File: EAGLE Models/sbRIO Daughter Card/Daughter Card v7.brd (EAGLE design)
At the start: 120.7 x 102.9 mm, 88 parts, among them IC1 BTS716G, IC2 BTS716G, IC3 BTS716G

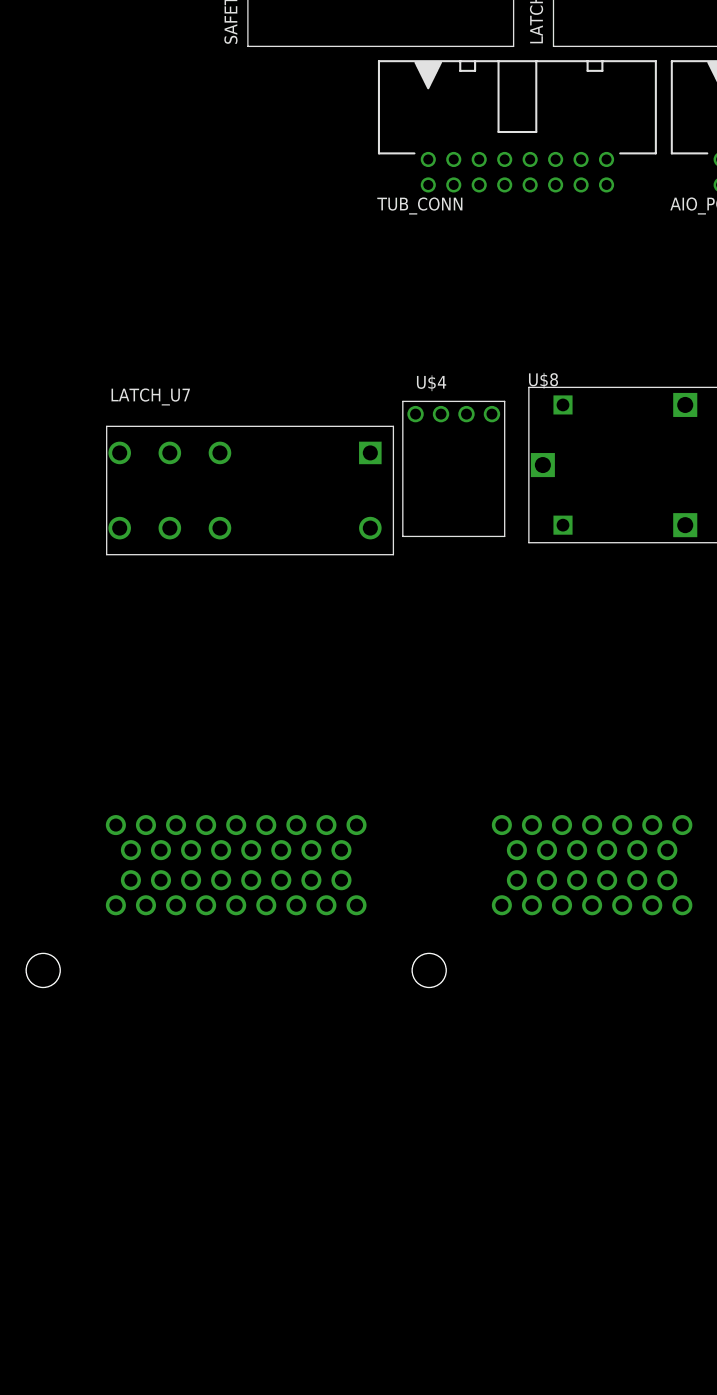
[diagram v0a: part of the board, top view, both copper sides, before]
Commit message: Began Seriously reworking Daughter card and tracing nets to new connectors
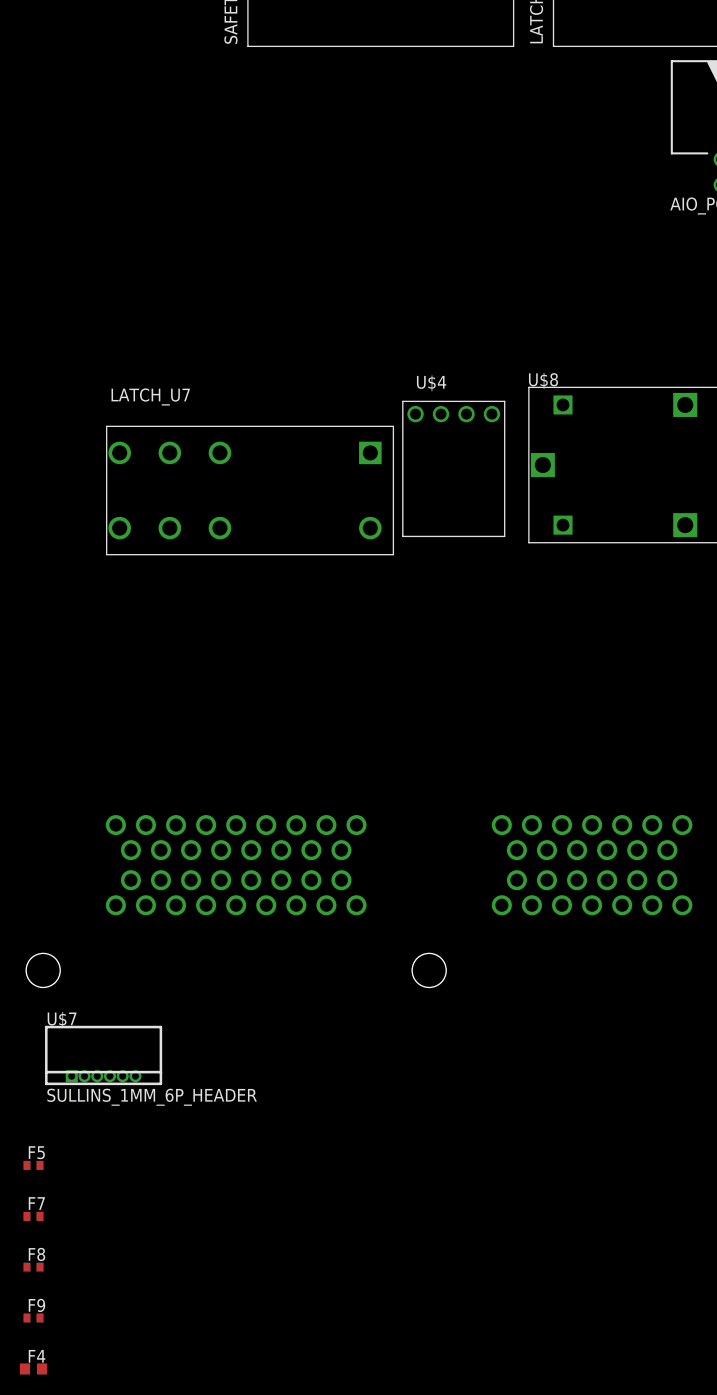
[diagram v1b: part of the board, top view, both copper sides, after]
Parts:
- removed TUB_CONN: 2516-5, con-3m:PAK100/2500-5-16
- added F4: 0.5A PTC, resistor:R0603
- added F5, F7, F8, F9: 10mA PTC, resistor:R0402
- added U$7: SULLINS_1MM_6P_HEADER, formula electric:SULLINS_1MM_HEADER
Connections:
- new net BRAKELIGHT: U$6.A17
- new net COOLANT_PUMP: AIO_PO_CONN.13
- new net FAN_PWM_OUT: AIO_PO_CONN.16
- new net N$11: U$6.A22
- new net N$12: F4.2
- new net N$15: U$6.B3
- new net N$16: U$6.A4
- new net N$17: U$6.A5
- new net N$18: U$6.A6
- new net N$19: U$6.A7
- new net N$21: U$6.A8
- new net N$22: U$6.A9
- new net N$23: U$6.B4
- new net N$24: U$6.B5
- new net N$25: U$6.B6
- new net N$26: U$6.B7
- new net N$28: U$6.A19
- new net N$30: U$6.A20
- new net N$31: U$6.B9
- new net N$32: U$6.B10
- new net N$33: U$6.A23
- new net N$34: U$6.A24
- new net N$35: U$6.A25
- new net N$36: U$6.A26
- new net N$37: U$6.A27
- new net N$38: U$6.A28
- new net N$39: U$6.A29
- new net N$40: U$6.A30
- new net N$42: U$6.A31
- new net N$43: U$6.A32
- new net N$44: U$6.A33
- new net N$45: U$6.A34
- new net N$67: U$6.B11
- new net N$68: U$6.B12
- new net N$69: U$6.B13
- new net N$70: F5.2
- new net N$71: F7.2
- new net N$72: F8.2
- new net N$73: F9.2
- net 5V: now also F4.1
- net 5V_IO_1: no longer TUB_CONN.3
- net ACCUMULATOR_FANS: now also AIO_PO_CONN.15; no longer AIO_PO_CONN.16
- net AI7: now also U$6.A11; no longer TUB_CONN.15
- net AMS_OUT: no longer TUB_CONN.6
- net AO0: now also F5.1
- net AO1: now also F7.1
- net AO2: now also F8.1
- net AO3: now also F9.1
- net BRAKE_PRESS_IN_1: now also U$6.A15; no longer TUB_CONN.11
- net BRAKE_PRESS_IN_2: now also U$6.A14; no longer TUB_CONN.12
- net BSPD_OUT: no longer TUB_CONN.4
- net BUZZER_OUT: now also U$6.A16; no longer TUB_CONN.7
- net CAN_GND: now also U$6.A3; no longer TUB_CONN.10
- net CAN_H: now also U$6.A1, U$6.B1; no longer TUB_CONN.9
- net CAN_L: now also U$6.A2, U$6.B2; no longer TUB_CONN.8
- net DC_DC_DISABLE: now also U$6.B8; no longer TUB_CONN.1
- net IMD_OUT: no longer TUB_CONN.5
- net LAP_TIMER_IN: now also U$6.A21; no longer TUB_CONN.2
- net LATCH_OK: no longer AIO_PO_CONN.8
- net PO2: now also U$6.A18; no longer AIO_PO_CONN.15
- net PO4: no longer AIO_PO_CONN.13
- net PRECHARGE_DONE+: now also AIO_PO_CONN.8
- net STEERING_POS: now also U$6.A10; no longer TUB_CONN.16
- net THROTTLE_IN_1: now also U$6.A13; no longer TUB_CONN.13
- net THROTTLE_IN_2: now also U$6.A12; no longer TUB_CONN.14

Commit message: Worked more on remapping connectors on daughter card
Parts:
- removed AIO_PO_CONN: 2516-5, con-3m:PAK100/2500-5-16
- removed AMS_U5, BSPD_U4, IMD_U6, INTERLOCKS_U3, SBRIO_U1, SBRIO_U2: HE3621A1250_SPST, formula electric:HE3621A1250_SPST
- removed F14, F2: 250mA, resistor:R0603
- removed F15, F20, F21, F22: 10mA PTC, resistor:R0402
- removed F16: 0.5A PTC, resistor:R0603
- removed F3: FUSEX20MM, SparkFun-Passives:FUSE_5MM
- removed LATCH_CONN, SAFETY_CONN: CONN_5, formula electric:CONNECTOR_5
- removed LATCH_U7: JW2SN-DC12V, formula electric:DPDT_JW2_FORM_C
- removed TSMS_CONN: CONN_2, formula electric:CONNECTOR_2
- removed U$1, U$2: DIODE_MMBD4448, formula electric:SOT-23-3
- removed U$8: RELAY, formula electric:RELAY
- added D7, D8: DIODE_MMBD4448, formula electric:SOT-23-3
- added F10, F11: 250mA, resistor:R0603
- added F12: FUSEX20MM, SparkFun-Passives:FUSE_5MM
- added GLV+_CONN, TSMS_CONN1: CONN_2, formula electric:CONNECTOR_2
- added K1, K2, K3, K4, K5, K6: HE3621A1250_SPST, formula electric:HE3621A1250_SPST
- added LATCH_CONN1, SAFETY_CONN1: CONN_5, formula electric:CONNECTOR_5
- added LATCH_U1: JW2SN-DC12V, formula electric:DPDT_JW2_FORM_C
- added U$9: RELAY, formula electric:RELAY
- 4401-7-F(1), 4401-7-F(2), 4403-7-F, 4403-7-F(2), 5225-3.3M5-TR(5), 5238B-7-F, 5525-3.3YM5-TR(1), 5525-3.3YM5-TR(2), 5525-3.3YM5-TR(3), 5525-3.3YM5-TR(4): device formula electric:SOT-23-3 -> formula electric:SOT-23-3@1
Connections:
- removed net COOLANT_PUMP: AIO_PO_CONN.13
- removed net FAN_PWM_OUT: AIO_PO_CONN.16
- removed net N$13: AMS_U5.S2, IMD_U6.S1
- removed net N$14: F3.1, F3.2, U$8.A
- removed net N$16: U$6.A4
- removed net N$17: U$6.A5
- removed net N$18: U$6.A6
- removed net N$19: U$6.A7
- removed net N$2: SBRIO_U1.S2, SBRIO_U2.S1
- removed net N$20: AIO_PO_CONN.2, F16.2
- removed net N$21: U$6.A8
- removed net N$22: U$6.A9
- removed net N$29: AIO_PO_CONN.3
- removed net N$44: U$6.A33
- removed net N$7: INTERLOCKS_U3.S1, SBRIO_U2.S2
- removed net N$8: AMS_U5.S1, BSPD_U4.S2
- removed net SBRIO_OK+_1_RELAY_IN: F2.2, SBRIO_U1.C+
- removed net SBRIO_OK_2_RELAY: F14.2, SBRIO_U2.C+
- new net K4: K4.S2, K5.S1
- new net N$46: U$6.B14
- new net N$47: U$6.B15
- new net N$48: U$6.B16
- new net N$49: U$6.B17
- new net N$50: U$6.B18
- new net N$51: U$6.B19
- new net N$53: U$6.B22
- new net N$55: U$6.B23
- new net N$59: U$6.B24
- new net N$65: U$6.B26
- new net SBRIO_OK+_1_RELAY_IN1: F10.2, K3.C+
- new net SBRIO_OK_2_RELAY1: F11.2, K2.C+
- net 5V: no longer F16.1
- net ACCUMULATOR_FANS: no longer AIO_PO_CONN.15
- net AI10: now also U$6.A6; no longer AIO_PO_CONN.7
- net AI8: now also U$6.A8; no longer AIO_PO_CONN.5
- net AI9: now also U$6.A7; no longer AIO_PO_CONN.6
- net AMS_OK-: now also K5.C-, SAFETY_CONN1.3, SAFETY_CONN1.4; no longer AMS_U5.C+, SAFETY_CONN.3, SAFETY_CONN.4
- net AO0: no longer F15.1
- net AO1: no longer F20.1
- net AO2: no longer F21.1
- net AO3: no longer F22.1
- net BSPD_OK+: now also K4.C+, SAFETY_CONN1.10, SAFETY_CONN1.9; no longer BSPD_U4.C+, SAFETY_CONN.1, SAFETY_CONN.2
- net CAN_GND: no longer U$6.A3
- net CAN_H: now also U$6.A33, U$6.B20; no longer U$6.A1, U$6.B1
- net CAN_L: now also U$6.A34, U$6.B21; no longer U$6.A2, U$6.B2
- net E-STOP_OK: no longer AIO_PO_CONN.4
- net GLV+: now also F12.3, F12.4, GLV+_CONN.3, GLV+_CONN.4, K3.S1, K4.S1; no longer AMS_U5.C-, BSPD_U4.S1, F3.3, F3.4, SBRIO_U1.S1
- net GND: now also D7.P$2, D8.P$2, K1.C-, K2.C-, K3.C-, K4.C-, K6.C-, LATCH_CONN1.7, LATCH_CONN1.8, LATCH_U1.COIL_1, U$9.V1; no longer BSPD_U4.C-, IMD_U6.C-, INTERLOCKS_U3.C-, LATCH_CONN.7, LATCH_CONN.8, LATCH_U7.COIL_1, SBRIO_U1.C-, SBRIO_U2.C-, U$1.P$2, U$2.P$2, U$8.V1
- net IMD_OK+: now also K6.C+, SAFETY_CONN1.5, SAFETY_CONN1.6; no longer IMD_U6.C+, SAFETY_CONN.5, SAFETY_CONN.6
- net INTER_OK+: now also K1.C+, SAFETY_CONN1.7, SAFETY_CONN1.8; no longer INTERLOCKS_U3.C+, SAFETY_CONN.7, SAFETY_CONN.8
- net LATCH_LED+: now also LATCH_CONN1.5, LATCH_CONN1.6, LATCH_U1.NC_2; no longer LATCH_CONN.5, LATCH_CONN.6, LATCH_U7.NC_2
- net LATCH_SW_IN: now also D7.P$1, LATCH_CONN1.1, LATCH_CONN1.2, LATCH_U1.COIL_2, LATCH_U1.NO_2; no longer LATCH_CONN.1, LATCH_CONN.2, LATCH_U7.COIL_2, LATCH_U7.NO_2, U$1.P$1
- net LATCH_SW_OUT: now also K6.S2, LATCH_CONN1.3, LATCH_CONN1.4, LATCH_U1.CENTER_2; no longer IMD_U6.S2, LATCH_CONN.3, LATCH_CONN.4, LATCH_U7.CENTER_2
- net N$10: now also F12.1, F12.2, U$9.A; no longer AIO_PO_CONN.12, F22.2
- net N$12: now also U$6.A9
- net N$3: now also K2.S1, K3.S2; no longer AIO_PO_CONN.9, F15.2
- net N$45: now also U$6.B2; no longer U$6.A34
- net N$6: now also K1.S1, K2.S2; no longer AIO_PO_CONN.10, F20.2
- net N$70: now also U$6.A4
- net N$71: now also U$6.A3
- net N$72: now also U$6.A2
- net N$73: now also U$6.A1
- net N$9: now also K5.S2, K6.S1; no longer AIO_PO_CONN.11, F21.2
- net PO3: now also K5.C+; no longer AIO_PO_CONN.14
- net PRECHARGE_DONE+: now also TSMS_CONN1.3, TSMS_CONN1.4, U$6.A5; no longer AIO_PO_CONN.8, TSMS_CONN.3, TSMS_CONN.4
- net SBRIO_OK+_1: now also F10.1; no longer F2.1
- net SBRIO_OK+_2: now also F11.1; no longer F14.1
- net SHUTDOWN_OK+: now also K1.S2, LATCH_U1.NO_1; no longer INTERLOCKS_U3.S2, LATCH_U7.NO_1
- net TSMS_IN+: now also TSMS_CONN1.1, TSMS_CONN1.2; no longer TSMS_CONN.1, TSMS_CONN.2
- net TSMS_OUT+: now also SAFETY_CONN1.1, SAFETY_CONN1.2, U$9.CENTER; no longer SAFETY_CONN.10, SAFETY_CONN.9, U$8.CENTER
- net TSMS_OUT_CTRL+: now also D8.P$1, LATCH_U1.CENTER_1, U$9.V2; no longer LATCH_U7.CENTER_1, U$2.P$1, U$8.V2

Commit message: Almost done remapping signals, and created board to start laying out
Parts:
- removed ACCUMULATOR_CONN: RJ45-6L21-S, con-tycoelectronics:RJ45-SHIELD1
- removed SBRIO_CAN: SBRIO_W500, formula electric:SBRIO_W
- added U$1: SBRIO_BMS_CONN, formula electric:SBRIO_W
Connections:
- removed net AI1: ACCUMULATOR_CONN.2, R24.2, SBRIO_ANALOG.P$6
- removed net AI2: ACCUMULATOR_CONN.3, BSPD_CONN.7, BSPD_CONN.8, R25.2, SBRIO_ANALOG.P$8
- removed net CAN_GND: ACCUMULATOR_CONN.1, ACCUMULATOR_CONN.S1, ACCUMULATOR_CONN.S2, ACCUMULATOR_CONN.S3, ACCUMULATOR_CONN.S4, SBRIO_CAN.P$3, SBRIO_CAN.P$6
- removed net N$36: U$6.A26
- removed net N$37: U$6.A27
- removed net SHIELD: ACCUMULATOR_CONN.6, SBRIO_CAN.P$10, SBRIO_CAN.P$5
- new net HIGH_CURRENT_IN: R24.2, SBRIO_ANALOG.P$6, U$6.A26
- new net LOW_CURRENT_IN: BSPD_CONN.7, BSPD_CONN.8, R25.2, SBRIO_ANALOG.P$8, U$6.A27
- new net N$13: U$1.P$7
- new net N$16: U$1.P$1
- new net N$17: U$1.P$2
- new net N$18: U$1.P$3
- new net N$19: U$1.P$4
- new net N$20: U$1.P$5
- new net N$8: U$1.P$8
- net AMS_OK_IN: no longer ACCUMULATOR_CONN.7
- net CAN_H: now also U$1.P$10; no longer ACCUMULATOR_CONN.5, SBRIO_CAN.P$7
- net CAN_L: now also U$1.P$9; no longer ACCUMULATOR_CONN.4, SBRIO_CAN.P$2
- net IMD_OK_IN: no longer ACCUMULATOR_CONN.8
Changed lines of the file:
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@@
 <attribute name="DIGIKEYPN" value="MCP1703T-3302E/CBCT-ND" x="-40.64" y="139.7" size="1.778" layer="27" display="off"/>
-</element>
-<element name="ACCUMULATOR_CONN" library="con-tycoelectronics" package="RJ45-SHIELD1" value="RJ45-6L21-S" x="-22.86" y="8.89">
-<attribute name="MPN" value="" x="-22.86" y="8.89" size="1.778" layer="27" display="off"/>
-<attribute name="MF" value="" x="-22.86" y="8.89" size="1.778" layer="27" display="off"/>
-<attribute name="OC_NEWARK" value="unknown" x="-22.86" y="8.89" size="1.778" layer="27" display="off"/>
-<attribute name="OC_FARNELL" value="unknown" x="-22.86" y="8.89" size="1.778" layer="27" display="off"/>
 </element>
 <element name="BSPD_CONN" library="formula electric" package="CONNECTOR_5" value="CONN_5" x="-36.83" y="58.42"/>
@@
 <element name="SBRIO_ANALOG" library="formula electric" package="SBRIO_J502_J503" value="SBRIO_MIO" x="-66.04" y="100.33"/>
 <element name="SBRIO_AUX" library="formula electric" package="SBRIO_J502_J503" value="SBRIO_AUX" x="-66.04" y="111.76"/>
-<element name="SBRIO_CAN" library="formula electric" package="SBRIO_W" value="SBRIO_W500" x="-68.58" y="87.63"/>
 <element name="SBRIO_MEZZANINE" library="SEAM-40-XX.X-XX-06-X-A" package="SEAM-40-XX.X-XX-06-X-A" value="SBRIO_RMC" x="-57.15" y="73.66"/>
 <element name="U$3" library="texas" package="SOT223-4" value="LM340MP-5.0" x="-91.44" y="71.12"/>
@@
 <element name="F12" library="SparkFun-Passives" package="FUSE_5MM" value="FUSEX20MM" x="-106.68" y="-110.49"/>
 <element name="GLV+_CONN" library="formula electric" package="CONNECTOR_2" value="CONN_2" x="-76.2" y="-182.88"/>
+<element name="U$1" library="formula electric" package="SBRIO_W" value="SBRIO_BMS_CONN" x="-109.22" y="-236.22"/>
 </elements>
 <signals>
@@
 </signal>
 <signal name="AMS_OK_IN">
-<contactref element="ACCUMULATOR_CONN" pad="7"/>
 <contactref element="5525-3.3YM5-TR(1)" pad="P$1"/>
 <contactref element="R1" pad="1"/>
 <wire x1="-78.12" y1="134.62" x2="-25.4" y2="140.7" width="0" layer="19" extent="1-1"/>
-<wire x1="-19.685" y1="15.24" x2="-25.4" y2="140.7" width="0" layer="19" extent="1-1"/>
 </signal>
 <signal name="DIO4">
@@
 </signal>
 <signal name="CAN_H">
-<contactref element="SBRIO_CAN" pad="P$7"/>
-<contactref element="ACCUMULATOR_CONN" pad="5"/>
 <contactref element="U$6" pad="A33"/>
 <contactref element="U$6" pad="B20"/>
+<contactref element="U$1" pad="P$10"/>
 <wire x1="-75.21" y1="-33.75" x2="-92.71" y2="-33.75" width="0" layer="19" extent="1-1"/>
-<wire x1="-22.225" y1="15.24" x2="-75.21" y2="-33.75" width="0" layer="19" extent="1-1"/>
-<wire x1="-66.04" y1="86.36" x2="-22.225" y2="15.24" width="0" layer="19" extent="1-1"/>
+<wire x1="-104.14" y1="-234.95" x2="-92.71" y2="-33.75" width="0" layer="19" extent="1-1"/>
 </signal>
 <signal name="CAN_L">
-<contactref element="SBRIO_CAN" pad="P$2"/>
-<contactref element="ACCUMULATOR_CONN" pad="4"/>
 <contactref element="U$6" pad="A34"/>
 <contactref element="U$6" pad="B21"/>
+<contactref element="U$1" pad="P$9"/>
 <wire x1="-72.21" y1="-33.75" x2="-89.71" y2="-33.75" width="0" layer="19" extent="1-1"/>
-<wire x1="-23.495" y1="17.78" x2="-72.21" y2="-33.75" width="0" layer="19" extent="1-1"/>
-<wire x1="-73.66" y1="88.9" x2="-23.495" y2="17.78" width="0" layer="19" extent="1-1"/>
-</signal>
-<signal name="CAN_GND">
-<contactref element="SBRIO_CAN" pad="P$3"/>
-<contactref element="SBRIO_CAN" pad="P$6"/>
-<contactref element="ACCUMULATOR_CONN" pad="1"/>
-<contactref element="ACCUMULATOR_CONN" pad="S4"/>
-<contactref element="ACCUMULATOR_CONN" pad="S3"/>
-<contactref element="ACCUMULATOR_CONN" pad="S2"/>
-<contactref element="ACCUMULATOR_CONN" pad="S1"/>
-<wire x1="-27.305" y1="15.24" x2="-30.988" y2="5.842" width="0" layer="19" extent="1-1"/>
-<wire x1="-30.988" y1="17.65" x2="-27.305" y2="15.24" width="0" layer="19" extent="1-1"/>
-<wire x1="-14.732" y1="17.65" x2="-27.305" y2="15.24" width="0" layer="19" extent="1-1"/>
-<wire x1="-14.732" y1="5.842" x2="-14.732" y2="17.65" width="0" layer="19" extent="1-1"/>
-<wire x1="-71.12" y1="86.36" x2="-30.988" y2="17.65" width="0" layer="19" extent="1-1"/>
-<wire x1="-68.58" y1="88.9" x2="-71.12" y2="86.36" width="0" layer="19" extent="1-1"/>
-</signal>
-<signal name="SHIELD">
-<contactref element="SBRIO_CAN" pad="P$5"/>
-<contactref element="SBRIO_CAN" pad="P$10"/>
-<contactref element="ACCUMULATOR_CONN" pad="6"/>
-<wire x1="-68.58" y1="86.36" x2="-63.5" y2="88.9" width="0" layer="19" extent="1-1"/>
-<wire x1="-20.955" y1="17.78" x2="-63.5" y2="88.9" width="0" layer="19" extent="1-1"/>
-</signal>
-<signal name="AI2">
+<wire x1="-104.14" y1="-237.49" x2="-89.71" y2="-33.75" width="0" layer="19" extent="1-1"/>
+</signal>
+<signal name="LOW_CURRENT_IN">
 <contactref element="SBRIO_ANALOG" pad="P$8"/>
 <contactref element="BSPD_CONN" pad="7"/>
 <contactref element="BSPD_CONN" pad="8"/>
-<contactref element="ACCUMULATOR_CONN" pad="3"/>
 <contactref element="R25" pad="2"/>
-<wire x1="-60.04" y1="102.33" x2="-66.66" y2="134.62" width="0" layer="19" extent="1-1"/>
-<wire x1="-19.33" y1="63.42" x2="-60.04" y2="102.33" width="0" layer="19" extent="1-1"/>
-<wire x1="-21.83" y1="58.42" x2="-19.33" y2="63.42" width="0" layer="19" extent="1-1"/>
-<wire x1="-24.765" y1="15.24" x2="-21.83" y2="58.42" width="0" layer="19" extent="1-1"/>
-</signal>
-<signal name="AI1">
+<contactref element="U$6" pad="A27"/>
+<wire x1="-21.83" y1="58.42" x2="-110.71" y2="-33.75" width="0" layer="19" extent="1-1"/>
+<wire x1="-19.33" y1="63.42" x2="-21.83" y2="58.42" width="0" layer="19" extent="1-1"/>
+<wire x1="-60.04" y1="102.33" x2="-19.33" y2="63.42" width="0" layer="19" extent="1-1"/>
+<wire x1="-66.66" y1="134.62" x2="-60.04" y2="102.33" width="0" layer="19" extent="1-1"/>
+</signal>
+<signal name="HIGH_CURRENT_IN">
 <contactref element="SBRIO_ANALOG" pad="P$6"/>
-<contactref element="ACCUMULATOR_CONN" pad="2"/>
 <contactref element="R24" pad="2"/>
-<wire x1="-62.04" y1="102.33" x2="-61.58" y2="134.62" width="0" layer="19" extent="1-1"/>
-<wire x1="-26.035" y1="17.78" x2="-62.04" y2="102.33" width="0" layer="19" extent="1-1"/>
+<contactref element="U$6" pad="A26"/>
+<wire x1="-62.04" y1="102.33" x2="-113.71" y2="-33.75" width="0" layer="19" extent="1-1"/>
+<wire x1="-61.58" y1="134.62" x2="-62.04" y2="102.33" width="0" layer="19" extent="1-1"/>
 </signal>
 <signal name="BRAKE_PRESS_IN_1">
@@
 </signal>
 <signal name="IMD_OK_IN">
-<contactref element="ACCUMULATOR_CONN" pad="8"/>
 <contactref element="5225-3.3M5-TR(5)" pad="P$1"/>
 <contactref element="R2" pad="1"/>
 <wire x1="-83.2" y1="134.62" x2="-45.72" y2="140.7" width="0" layer="19" extent="1-1"/>
-<wire x1="-18.415" y1="17.78" x2="-45.72" y2="140.7" width="0" layer="19" extent="1-1"/>
 </signal>
 <signal name="DIO20">
@@
 <contactref element="U$6" pad="A25"/>
 </signal>
-<signal name="N$36">
-<contactref element="U$6" pad="A26"/>
-</signal>
-<signal name="N$37">
-<contactref element="U$6" pad="A27"/>
-</signal>
 <signal name="N$38">
 <contactref element="U$6" pad="A28"/>
@@
 <wire x1="-77.47" y1="-198.12" x2="-105.83" y2="-220.98" width="0" layer="19" extent="1-1"/>
 </signal>
+<signal name="N$8">
+<contactref element="U$1" pad="P$8"/>
+</signal>
+<signal name="N$13">
+<contactref element="U$1" pad="P$7"/>
+</signal>
+<signal name="N$16">
+<contactref element="U$1" pad="P$1"/>
+</signal>
+<signal name="N$17">
+<contactref element="U$1" pad="P$2"/>
+</signal>
+<signal name="N$18">
+<contactref element="U$1" pad="P$3"/>
+</signal>
+<signal name="N$19">
+<contactref element="U$1" pad="P$4"/>
+</signal>
+<signal name="N$20">
+<contactref element="U$1" pad="P$5"/>
+</signal>
 </signals>
